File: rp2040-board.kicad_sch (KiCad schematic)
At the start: 101 parts, among them J1 USB_C, J10 E0-RUNOUT, J11 FAN1, J12 FAN2, J13 FAN3, J14 HB, J15 HE0, J16 HE0, J2 24V IN, J3 PGA2040, J4 GPIO_20-22, J5 PROBE, J6 X-ENDSTOP, J7 Y-ENDSTOP, J8 HB, J9 Z-ENDSTOP, Q1 AOSS32334C, Q2 AOSS32334C, Q3 AOSS32334C, SW1 SW_MEC_5E, U1 LD1086DT33TR, U2 TPS5450DDAR, U3 74HCT365D,653, U4 FDS8896, U5 FDS8896

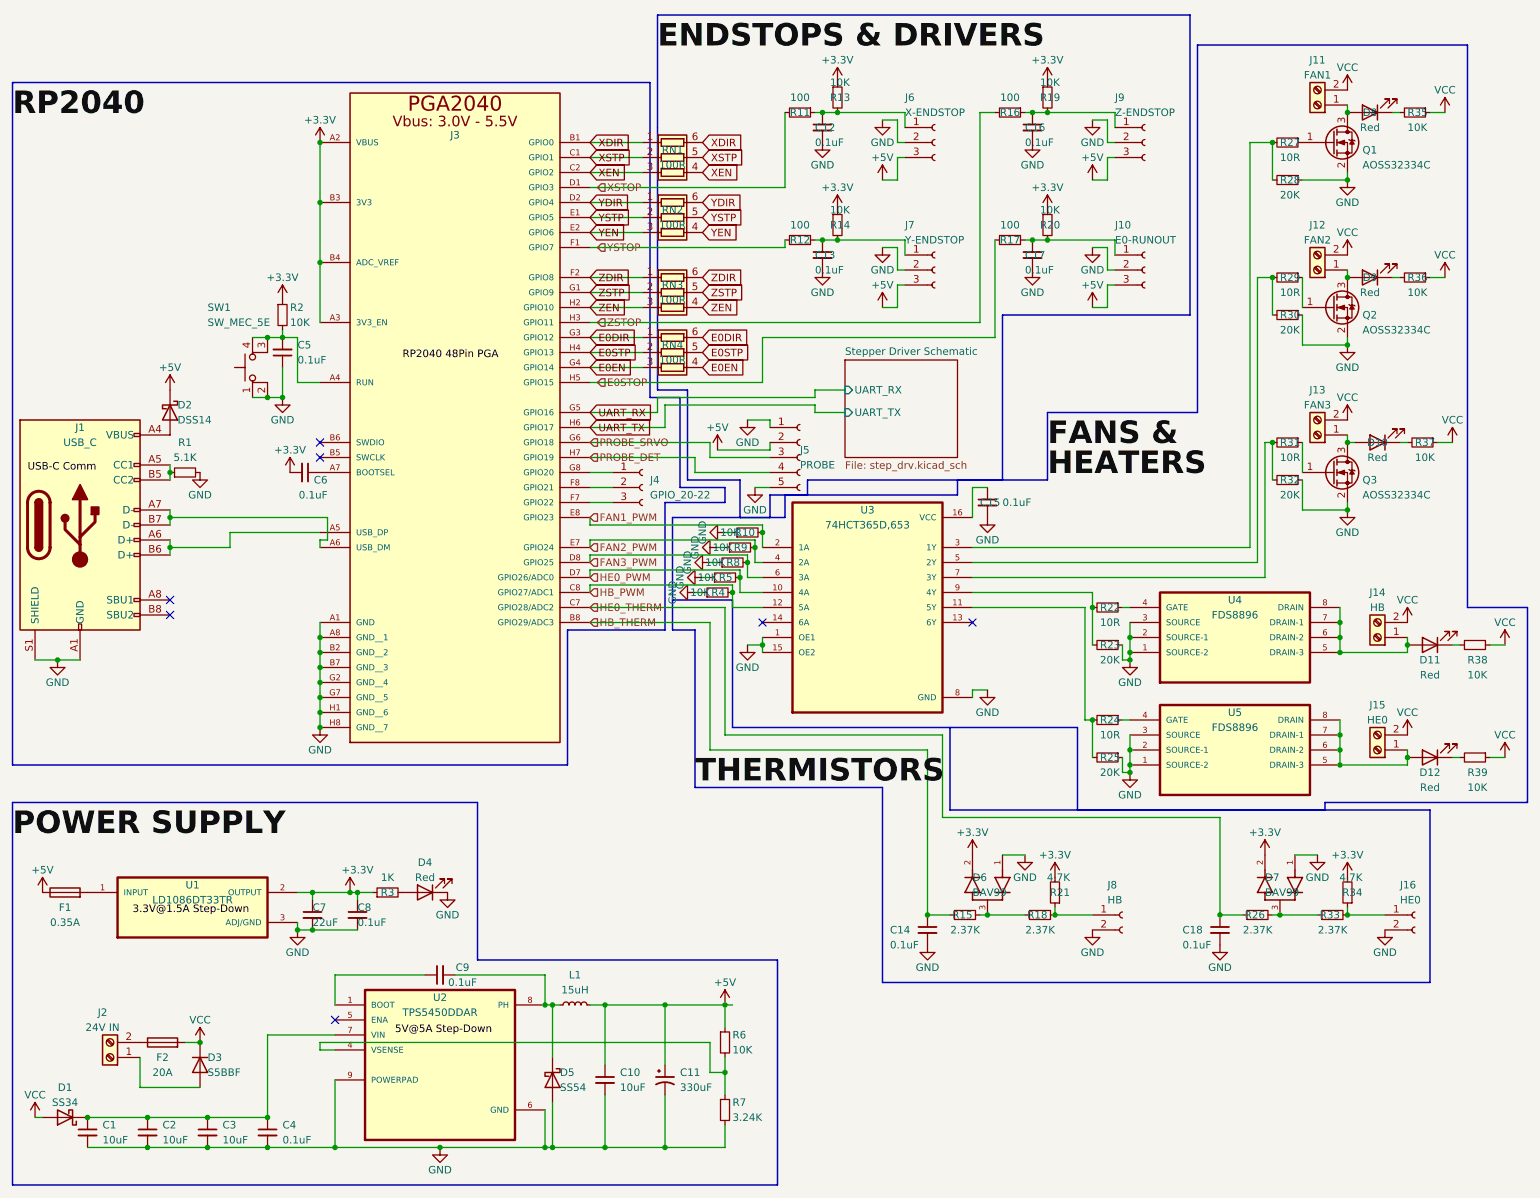
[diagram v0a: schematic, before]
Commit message: Minor Schematic Layout Changes
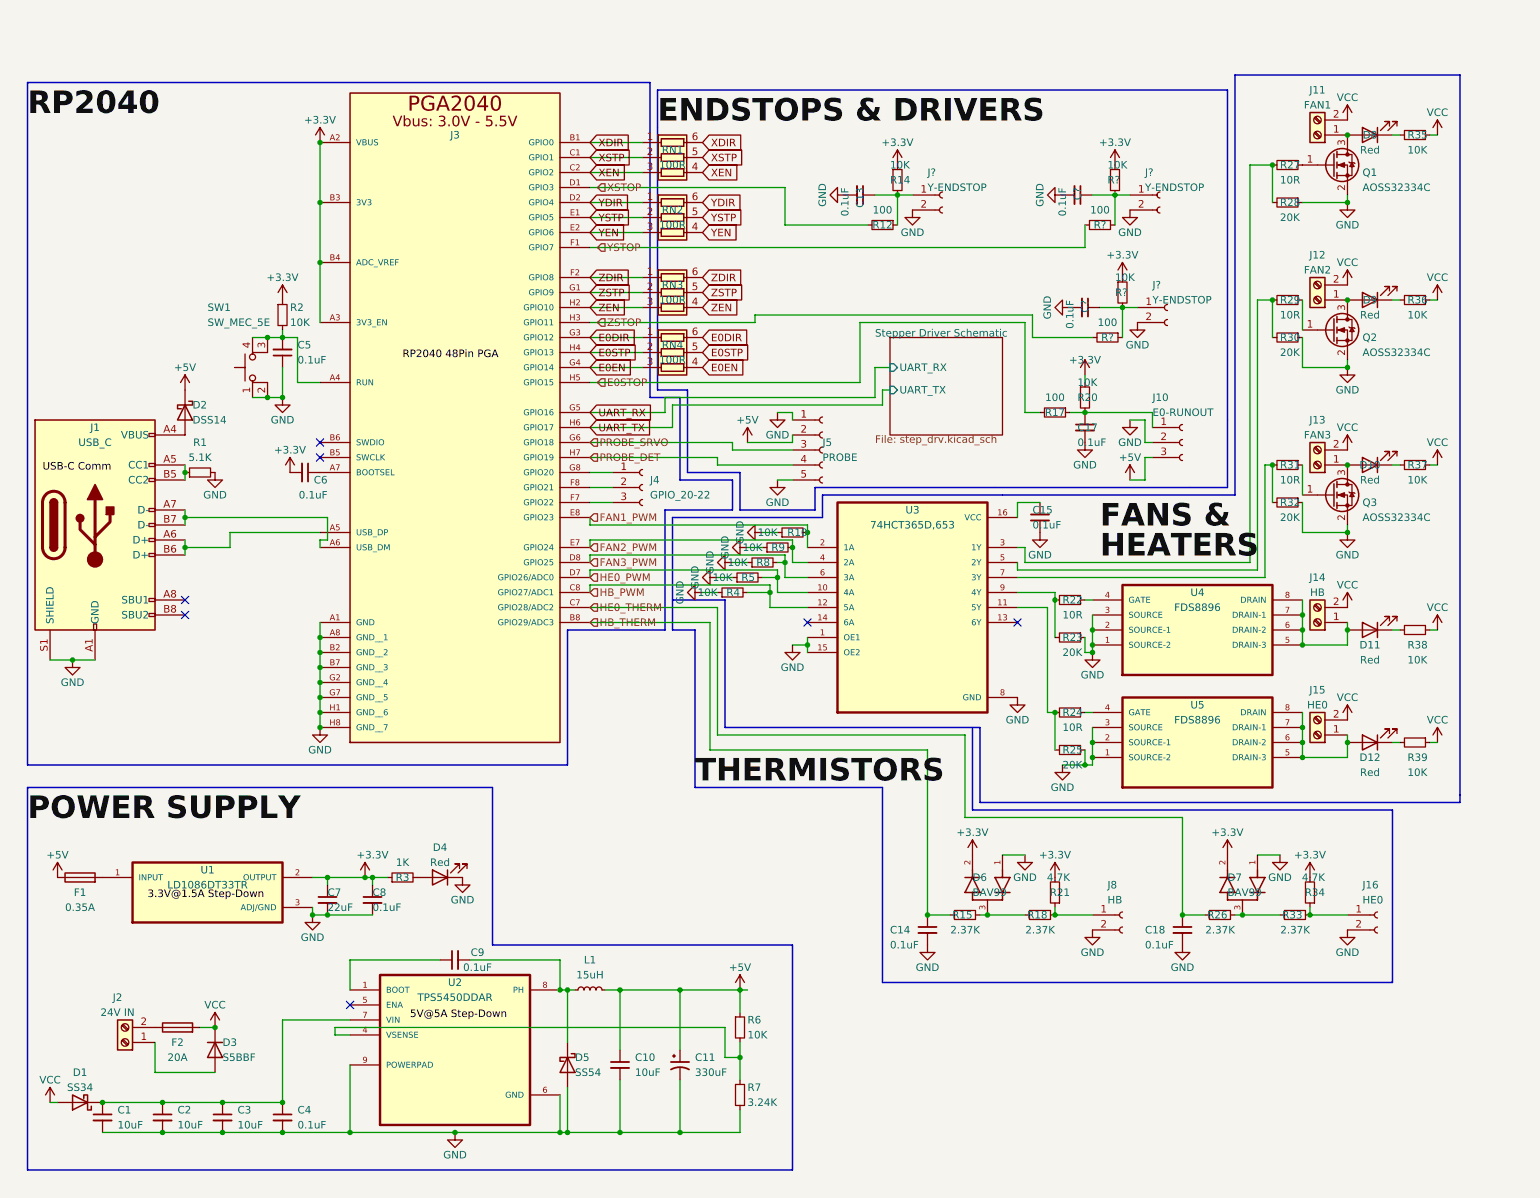
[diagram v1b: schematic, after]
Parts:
- removed C12, C16: 0.1uF, symbol Device:C_Small
- removed J6: X-ENDSTOP, Connector_JST:JST_XH_B3B-XH-A_1x03_P2.50mm_Vertical, symbol Connector:Conn_01x03_Female
- removed J7: Y-ENDSTOP, Connector_JST:JST_XH_B3B-XH-A_1x03_P2.50mm_Vertical, symbol Connector:Conn_01x03_Female
- removed J9: Z-ENDSTOP, Connector_JST:JST_XH_B3B-XH-A_1x03_P2.50mm_Vertical, symbol Connector:Conn_01x03_Female
- removed R11, R16: 100, symbol Device:R_Small
- removed R13, R19: 10K, symbol Device:R_Small
- added C? (x2): 0.1uF, symbol Device:C_Small
- added J? (x3): Y-ENDSTOP, Connector_JST:JST_XH_B2B-XH-A_1x02_P2.50mm_Vertical, symbol Connector:Conn_01x02_Female
- added R? (x2): 100, symbol Device:R_Small
- added R? (x2): 10K, symbol Device:R_Small
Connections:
- net +3.3V: now also R?.1, R?.1
- net GND: now also C?.2, C?.2, J?.2 (Pin_2), J?.2 (Pin_2), J?.2 (Pin_2)
- net HEATERS: now also R27.2, R28.2, U3.3 (1Y)
- net XSTOP: now also R12.2
- net YSTOP: now also R?.2; no longer R12.2
- net ZSTOP: now also R?.2
- net at C13.1, R12.1, R14.2: now also J?.1 (Pin_1)
- new net: C?.1, J?.1 (Pin_1), R?.1, R?.2 (x2)
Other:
- moved on the sheet: C1, C10, C11, C13, C15, C17, C18, C2, C3, C4, C7, C8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

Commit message: All components footprinted
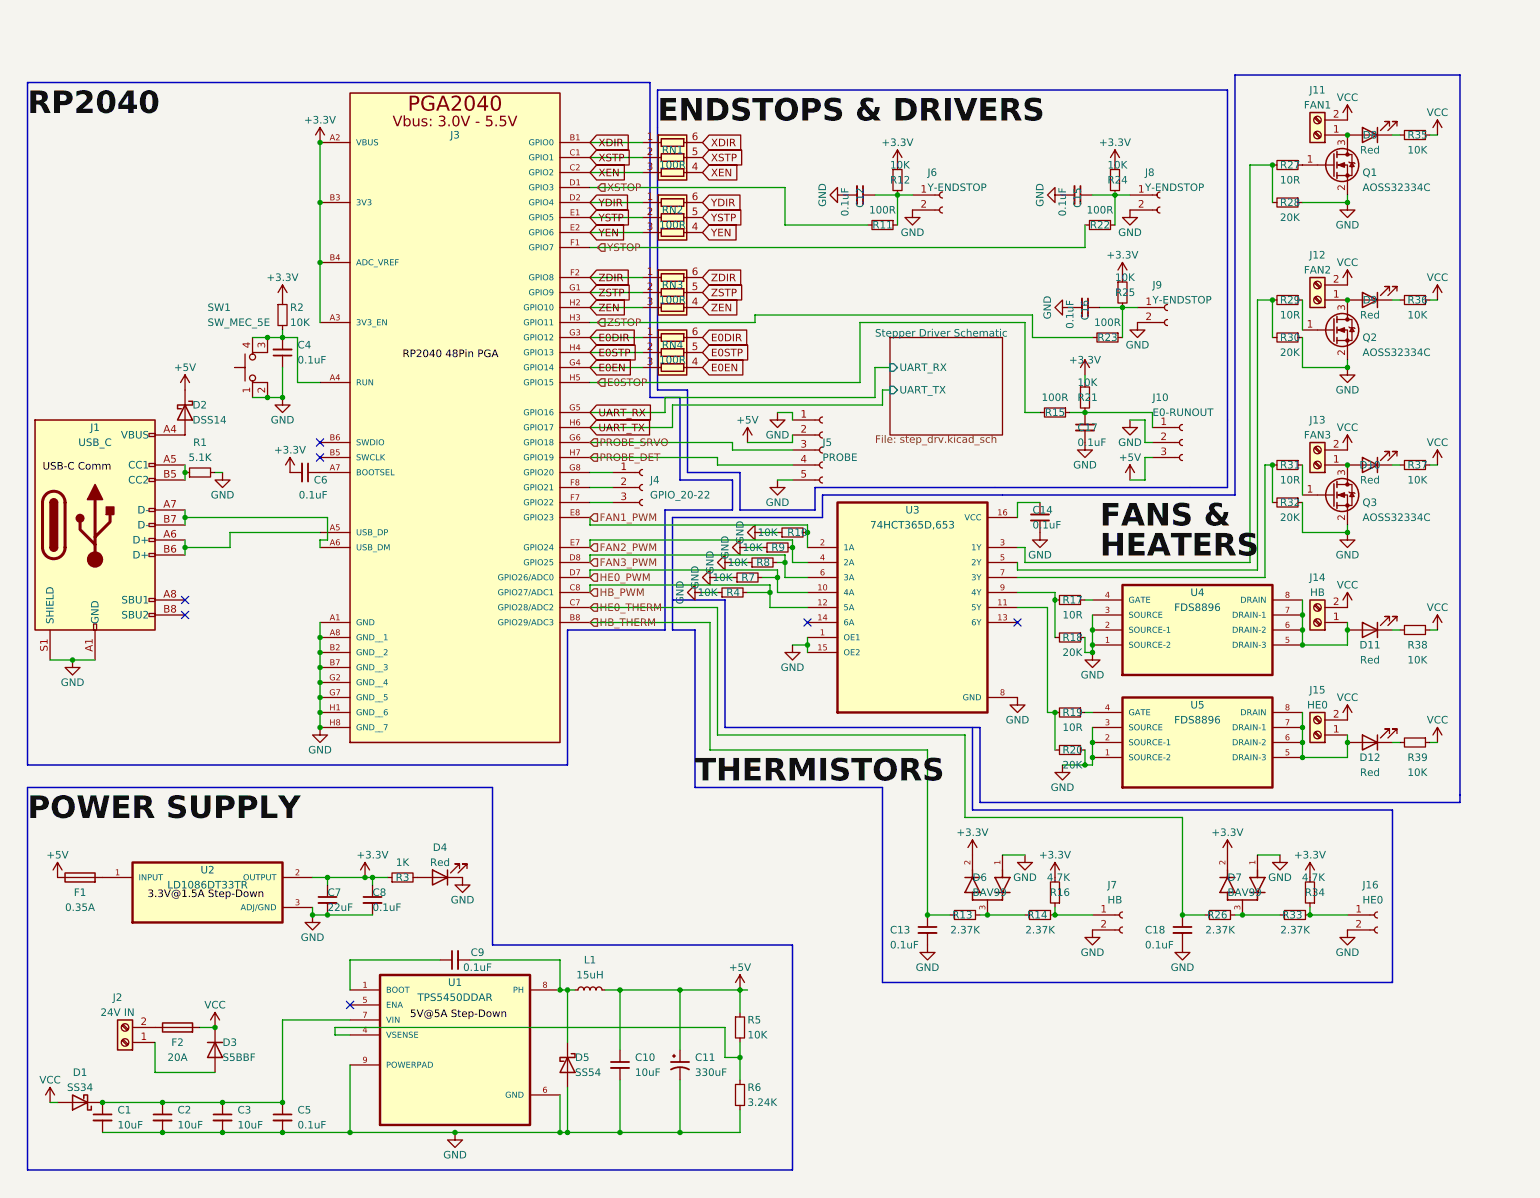
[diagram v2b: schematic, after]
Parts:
- C1, C10, C17, C18, C2, C3, C6, C7, C8, C9: footprint (none) -> Capacitor_SMD:C_1206_3216Metric_Pad1.33x1.80mm_HandSolder
- C11: footprint (none) -> Capacitor_THT:CP_Radial_D6.3mm_P2.50mm
- C12: renamed from C13; footprint (none) -> Capacitor_SMD:C_1206_3216Metric_Pad1.33x1.80mm_HandSolder
- C13: renamed from C14; footprint (none) -> Capacitor_SMD:C_1206_3216Metric_Pad1.33x1.80mm_HandSolder
- C14: renamed from C15; footprint (none) -> Capacitor_SMD:C_1206_3216Metric_Pad1.33x1.80mm_HandSolder
- C15, C16: renamed from C?; footprint (none) -> Capacitor_SMD:C_1206_3216Metric_Pad1.33x1.80mm_HandSolder
- C4: renamed from C5; footprint (none) -> Capacitor_SMD:C_1206_3216Metric_Pad1.33x1.80mm_HandSolder
- C5: renamed from C4; footprint (none) -> Capacitor_SMD:C_1206_3216Metric_Pad1.33x1.80mm_HandSolder
- D1, D10, D11, D12, D2, D3, D4, D5, D8, D9: footprint (none) -> Diode_SMD:D_1206_3216Metric_Pad1.42x1.75mm_HandSolder
- D6, D7: footprint DIO_BAV99 -> BAV99:DIO_BAV99
- F1: footprint (none) -> Fuse:Fuse_1812_4532Metric_Pad1.30x3.40mm_HandSolder
- F2: footprint (none) -> Fuse:Fuse_Blade_Mini_directSolder
- J11, J12, J13: footprint (none) -> Connector_JST:JST_XH_B2B-XH-A_1x02_P2.50mm_Vertical
- J14, J15, J2: footprint (none) -> TerminalBlock:TerminalBlock_bornier-2_P5.08mm
- L1: footprint (none) -> Inductor_SMD:L_1206_3216Metric_Pad1.22x1.90mm_HandSolder
- Q1, Q2, Q3: footprint Package_TO_SOT_SMD:SOT-23 -> Package_TO_SOT_SMD:SOT-23_Handsoldering
- R1, R10, R2, R26, R27, R28, R29, R3, R30, R31, R32, R33, R34, R35, R36, R37, R38, R39, R4, R8, R9: footprint (none) -> Resistor_SMD:R_1206_3216Metric_Pad1.30x1.75mm_HandSolder
- R11: renamed from R12; value 100 -> 100R; footprint (none) -> Resistor_SMD:R_1206_3216Metric_Pad1.30x1.75mm_HandSolder
- R12: renamed from R14; footprint (none) -> Resistor_SMD:R_1206_3216Metric_Pad1.30x1.75mm_HandSolder
- R13: renamed from R15; footprint (none) -> Resistor_SMD:R_1206_3216Metric_Pad1.30x1.75mm_HandSolder
- R14: renamed from R18; footprint (none) -> Resistor_SMD:R_1206_3216Metric_Pad1.30x1.75mm_HandSolder
- R15: renamed from R17; value 100 -> 100R; footprint (none) -> Resistor_SMD:R_1206_3216Metric_Pad1.30x1.75mm_HandSolder
- R16: renamed from R21; footprint (none) -> Resistor_SMD:R_1206_3216Metric_Pad1.30x1.75mm_HandSolder
- R17: renamed from R22; footprint (none) -> Resistor_SMD:R_1206_3216Metric_Pad1.30x1.75mm_HandSolder
- R18: renamed from R23; footprint (none) -> Resistor_SMD:R_1206_3216Metric_Pad1.30x1.75mm_HandSolder
- R19: renamed from R24; footprint (none) -> Resistor_SMD:R_1206_3216Metric_Pad1.30x1.75mm_HandSolder
- R20: renamed from R25; footprint (none) -> Resistor_SMD:R_1206_3216Metric_Pad1.30x1.75mm_HandSolder
- R21: renamed from R20; footprint (none) -> Resistor_SMD:R_1206_3216Metric_Pad1.30x1.75mm_HandSolder
- R22, R23: renamed from R?; value 100 -> 100R; footprint (none) -> Resistor_SMD:R_1206_3216Metric_Pad1.30x1.75mm_HandSolder
- R24, R25: renamed from R?; footprint (none) -> Resistor_SMD:R_1206_3216Metric_Pad1.30x1.75mm_HandSolder
- R5: renamed from R6; footprint (none) -> Resistor_SMD:R_1206_3216Metric_Pad1.30x1.75mm_HandSolder
- R6: renamed from R7; footprint (none) -> Resistor_SMD:R_1206_3216Metric_Pad1.30x1.75mm_HandSolder
- R7: renamed from R5; footprint (none) -> Resistor_SMD:R_1206_3216Metric_Pad1.30x1.75mm_HandSolder
- RN1, RN2, RN3, RN4: footprint (none) -> Resistor_SMD:R_Array_Convex_4x1206
- SW1: footprint (none) -> Button_Switch_SMD:SW_Push_1P1T_NO_CK_KSC6xxJ
- U1: renamed from U2; footprint VREG_LM5017MR/NOPB -> TPS5450:VREG_LM5017MR_NOPB
- U2: renamed from U1; footprint VREG_L78M08CDT-TR -> LD1086DT33TR:VREG_L78M08CDT-TR
- U3: footprint SOIC127P600X175-16N -> 74HCT365D_653:SOIC127P600X175-16N
- U4, U5: footprint SOIC127P600X175-8N -> FDS8896:SOIC127P600X175-8N
- gave numbers to parts that had none: 3
- renumbered J8 to J7

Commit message: BOM 99% done
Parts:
- removed D2: DSS14, Diode_SMD:D_1206_3216Metric_Pad1.42x1.75mm_HandSolder, symbol Device:D_Schottky
- removed J1: USB_C, Connector_USB:USB_C_Receptacle_HRO_TYPE-C-31-M-12, symbol Connector:USB_C_Receptacle_USB2.0
- added J2: USB4105-GF-A, USB4105_GCT, symbol ul_USB4105-GF-A:USB4105-GF-A
- C1, C10, C12, C13, C14, C15, C16, C17, C18, C2, C3, C4, C5, C6, C8, C9: MANUFACTURER (none) -> Samsung
- C11, C7, R1, R10, R11, R12, R13, R14, R15, R16, R17, R18, R19, R2, R20, R21, R22, R23, R24, R25, R26, R27, R28, R29, R3, R30, R31, R32, R33, R34, R35, R36, R37, R38, R39, R4, R5, R6, R7, R8, R9: MANUFACTURER (none) -> Panasonic
- D1: footprint Diode_SMD:D_1206_3216Metric_Pad1.42x1.75mm_HandSolder -> Diode_SMD:D_SMC_Handsoldering; MANUFACTURER (none) -> onsemi
- D10: renamed from D11; value Red -> Red LED; footprint Diode_SMD:D_1206_3216Metric_Pad1.42x1.75mm_HandSolder -> Diode_SMD:D_1210_3225Metric_Pad1.42x2.65mm_HandSolder; MANUFACTURER (none) -> American Bright Optoelectronics
- D11: renamed from D12; value Red -> Red LED; footprint Diode_SMD:D_1206_3216Metric_Pad1.42x1.75mm_HandSolder -> Diode_SMD:D_1210_3225Metric_Pad1.42x2.65mm_HandSolder; MANUFACTURER (none) -> American Bright Optoelectronics
- D3: renamed from D4; value Red -> Red LED; footprint Diode_SMD:D_1206_3216Metric_Pad1.42x1.75mm_HandSolder -> Diode_SMD:D_1210_3225Metric_Pad1.42x2.65mm_HandSolder; MANUFACTURER (none) -> American Bright Optoelectronics
- D5: renamed from D6; MANUFACTURER On Semi -> SMC Diode Solutions
- D6: renamed from D7; MANUFACTURER On Semi -> SMC Diode Solutions
- D7: renamed from D8; value Red -> Red LED; footprint Diode_SMD:D_1206_3216Metric_Pad1.42x1.75mm_HandSolder -> Diode_SMD:D_1210_3225Metric_Pad1.42x2.65mm_HandSolder; MANUFACTURER (none) -> American Bright Optoelectronics
- D8: renamed from D9; value Red -> Red LED; footprint Diode_SMD:D_1206_3216Metric_Pad1.42x1.75mm_HandSolder -> Diode_SMD:D_1210_3225Metric_Pad1.42x2.65mm_HandSolder; MANUFACTURER (none) -> American Bright Optoelectronics
- D9: renamed from D10; value Red -> Red LED; footprint Diode_SMD:D_1206_3216Metric_Pad1.42x1.75mm_HandSolder -> Diode_SMD:D_1210_3225Metric_Pad1.42x2.65mm_HandSolder; MANUFACTURER (none) -> American Bright Optoelectronics
- F1: MANUFACTURER (none) -> YAGEO
- F2: MANUFACTURER (none) -> Littelfuse
- J1: renamed from J2; footprint TerminalBlock:TerminalBlock_bornier-2_P5.08mm -> 1825966-1:SW_1825966-1; MANUFACTURER (none) -> Phoneix Contact
- J10, J11, J12, J13, J16, J5, J6, J7, J8, J9: MANUFACTURER (none) -> JST Sales
- J14, J15: footprint TerminalBlock:TerminalBlock_bornier-2_P5.08mm -> 1825966-1:SW_1825966-1; MANUFACTURER (none) -> Phoneix Contact
- J3: MANUFACTURER (none) -> Pimoroni
- J4: MANUFACTURER (none) -> Molex
- L1: footprint Inductor_SMD:L_1206_3216Metric_Pad1.22x1.90mm_HandSolder -> Inductor_SMD:L_1210_3225Metric_Pad1.42x2.65mm_HandSolder; MANUFACTURER (none) -> Taiyo Yuden
- Q1, Q2, Q3: MANUFACTURER (none) -> Alpha & Omega Semiconductor; Manufacturer (none) -> Alpha & Omega Semiconductor
- RN1, RN2, RN3, RN4: MANUFACTURER (none) -> Bourns
- SW1: MANUFACTURER (none) -> TE Connectivity
- U1: renamed from U2; MANUFACTURER (none) -> STMicroelectronics
- U2: renamed from U1; MANUFACTURER (none) -> Texas Instruments; Manufacturer (none) -> Texas Instruments
- U3: MANUFACTURER (none) -> Nexperia USA
- U4, U5: MANUFACTURER (none) -> onsemi
- renumbered D3 to D2, D5 to D4
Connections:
- net GND: now also J2.A1-B12 (GND), J2.B1-A12 (GND)
- net at R1.1: now also J2.A5 (CC1), J2.B5 (CC2)
- net at J3.A5 (USB_DP): now also J2.A6 (DP1), J2.B6 (DP2)
- net at J3.A6 (USB_DM): now also J2.A7 (DN1), J2.B7 (DN2)
- no-connect marks 7 -> 9

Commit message: Totally no 80% re-source of the BOM
suuurely no re-source
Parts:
- C1, C10, C12, C13, C14, C15, C16, C17, C18, C2, C3, C6, C8, C9: MANUFACTURER Samsung -> Murata
- C11: footprint Capacitor_THT:CP_Radial_D6.3mm_P2.50mm -> Capacitor_THT:CP_Radial_D8.0mm_P3.50mm
- C4: renamed from C5; MANUFACTURER Samsung -> Murata
- C5: renamed from C4; MANUFACTURER Samsung -> Murata
- C7: footprint Capacitor_SMD:C_1206_3216Metric_Pad1.33x1.80mm_HandSolder -> Capacitor_SMD:C_1210_3225Metric_Pad1.33x2.70mm_HandSolder; MANUFACTURER Panasonic -> Taiyo Yuden
- D2: footprint Diode_SMD:D_1206_3216Metric_Pad1.42x1.75mm_HandSolder -> Diode_SMD:D_SMB-SMC_Universal_Handsoldering; MANUFACTURER (none) -> Shikues; Spice_Netlist_Enabled Y -> (none); Spice_Primitive D -> (none)
- D4: footprint Diode_SMD:D_1206_3216Metric_Pad1.42x1.75mm_HandSolder -> Diode_SMD:D_SMC_Handsoldering; MANUFACTURER (none) -> Micro Commericial Co.
- D5, D6: MAXIMUM_PACKAGE_HEIGHT 1.2 mm -> (none); PARTREV 1.1.0 -> (none); SNAPEDA_PN BAV99 -> (none); STANDARD Manufacturer Recommendations -> (none)
- F2: footprint Fuse:Fuse_Blade_Mini_directSolder -> 01000063Z:01000063Z
- J1, J14: footprint 1825966-1:SW_1825966-1 -> TerminalBlock_Phoenix:TerminalBlock_Phoenix_MKDS-1,5-2_1x02_P5.00mm_Horizontal; MANUFACTURER Phoneix Contact -> DIBO
- J11, J12, J13, J8: MANUFACTURER JST Sales -> HCTL
- J15: value HE0 -> E0; footprint 1825966-1:SW_1825966-1 -> TerminalBlock_Phoenix:TerminalBlock_Phoenix_MKDS-1,5-2_1x02_P5.00mm_Horizontal; MANUFACTURER Phoneix Contact -> DIBO
- J16: value HE0 -> TH-E0; MANUFACTURER JST Sales -> HCTL
- J2: footprint USB4105_GCT -> ul_USB4105-GF-A:USB4105-GF-A; MANUFACTURER (none) -> GCT
- J4: value GPIO_20-22 -> 3_GPIO; MANUFACTURER Molex -> HCTL
- J5: MANUFACTURER JST Sales -> BOOMELE
- J6: value Y-ENDSTOP -> X-ENDSTOP; MANUFACTURER JST Sales -> HCTL
- J7: value HB -> TH-HB; MANUFACTURER JST Sales -> HCTL
- J9: value Y-ENDSTOP -> Z-ENDSTOP; MANUFACTURER JST Sales -> HCTL
- Q1, Q2, Q3: value AOSS32334C -> AO3400C; Manufacturer Alpha & Omega Semiconductor -> (none)
- R10, R11, R12, R15, R16, R2, R21, R22, R23, R24, R25, R34, R35, R36, R37, R38, R39, R4, R5, R7, R8, R9: MANUFACTURER Panasonic -> Vishay Intertech
- R13, R14, R26, R33, R6: footprint Resistor_SMD:R_1206_3216Metric_Pad1.30x1.75mm_HandSolder -> Resistor_SMD:R_1210_3225Metric_Pad1.30x2.65mm_HandSolder; MANUFACTURER Panasonic -> YAGEO
- R17, R19, R27, R29, R3, R31: MANUFACTURER Panasonic -> YAGEO
- U1: Manufacturer STMicroelectronics -> (none); Package VREG_L78M08CDT-TR -> (none)
- U2: Manufacturer Texas Instruments -> (none)
- U3: Manufacturer Nexperia USA -> (none); Package SOIC127P600X175-16N -> (none)
- U4, U5: Manufacturer ON Semiconductor -> (none); Package SOIC127P600X175-8N -> (none)
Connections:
- net HE0_PWM renamed E0_PWM
- net HE0_THERM renamed E0_THERM
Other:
- moved on the sheet: C5, C6, J2, R1, R2, SW1
